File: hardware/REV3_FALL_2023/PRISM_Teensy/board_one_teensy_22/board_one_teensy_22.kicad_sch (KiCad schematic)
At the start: 19 parts, among them J1 EAST, J2 CORE_IO, J3 USB_micro, U1 Teensy4.1, U2 BNO055_Breakout, U3 3966

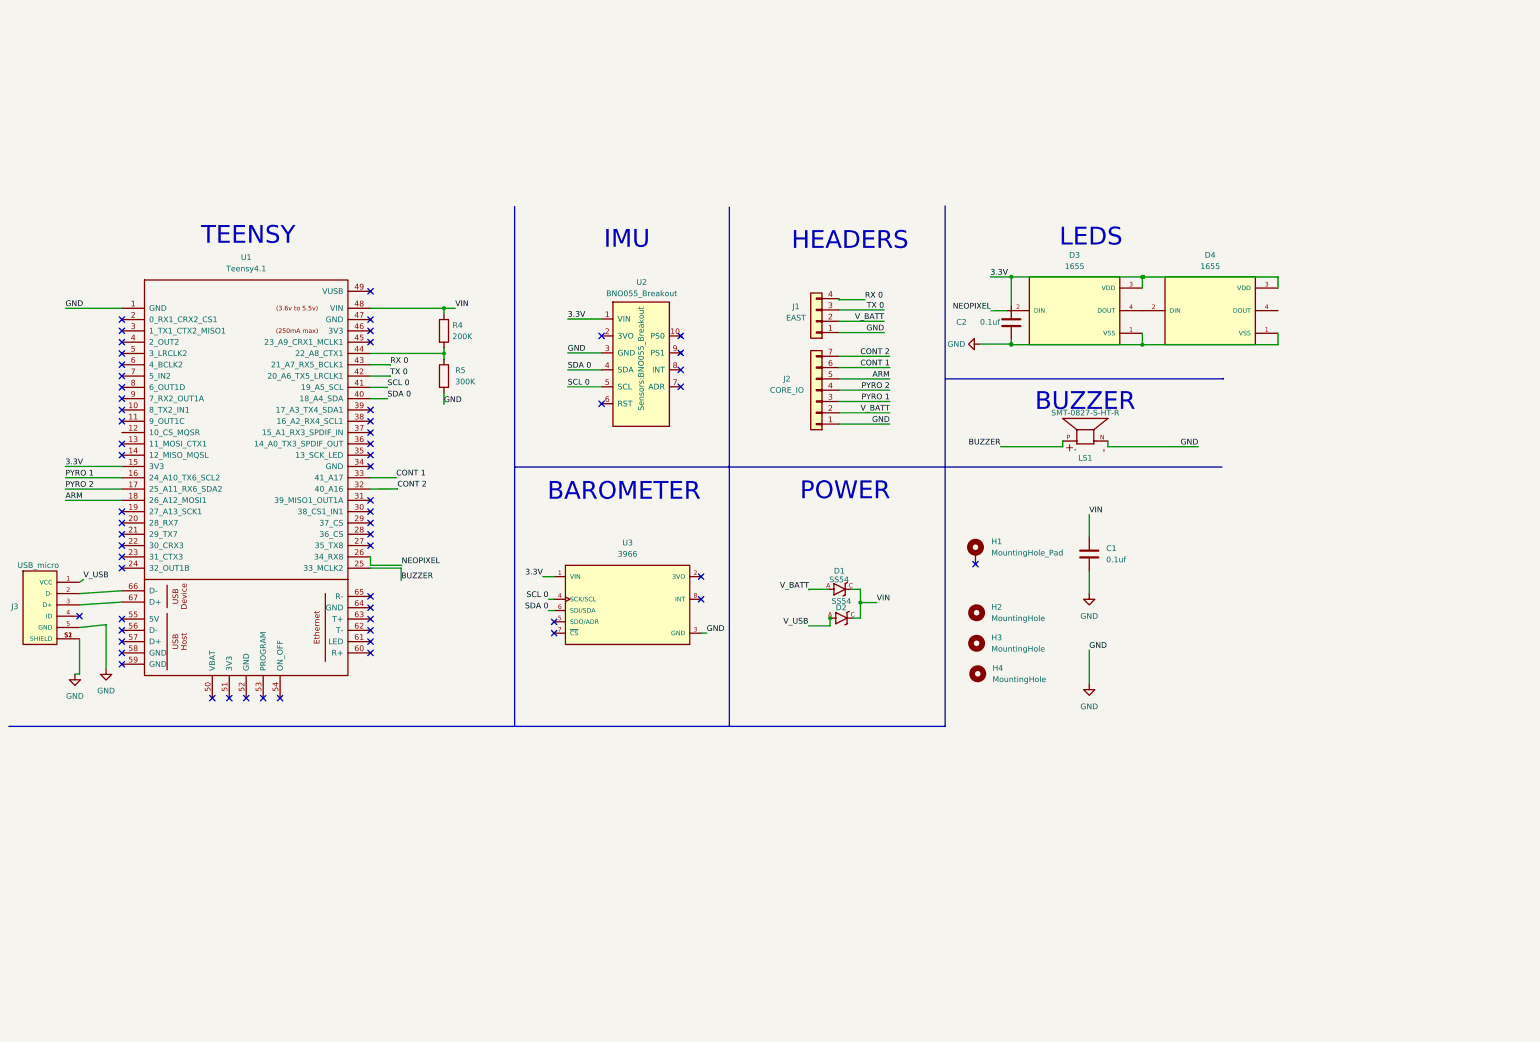
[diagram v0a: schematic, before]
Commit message: added teensy 4.0 and new connector spec
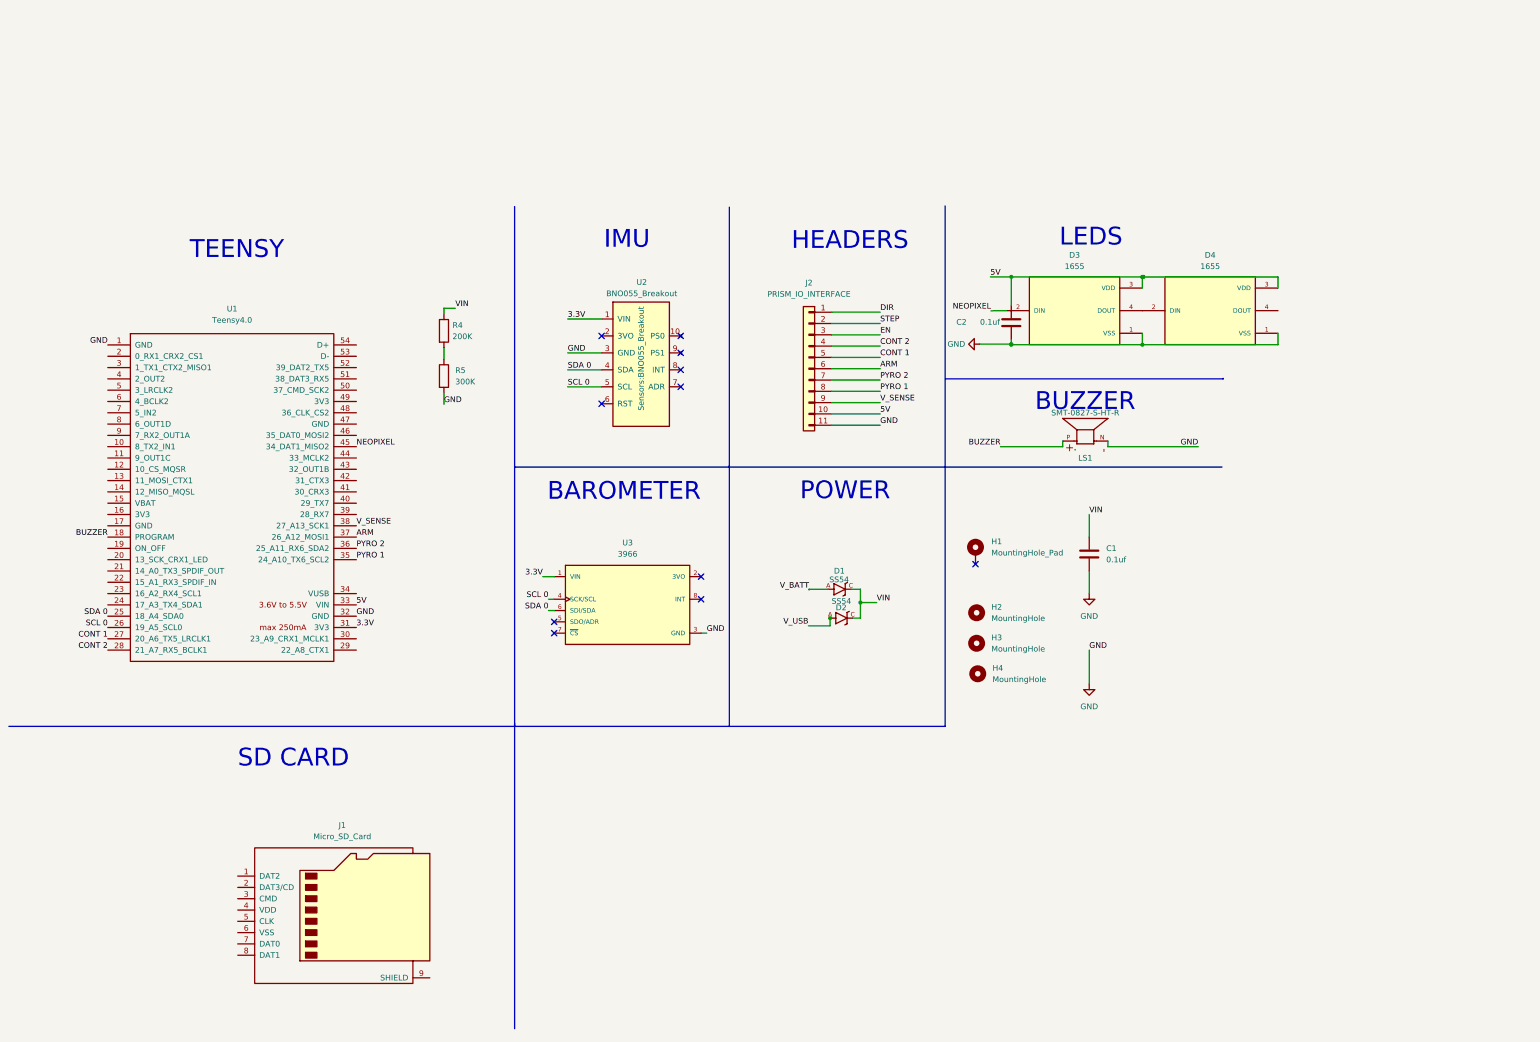
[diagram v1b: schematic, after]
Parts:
- removed J1: EAST, Connector_JST:JST_PH_S4B-PH-K_1x04_P2.00mm_Horizontal, symbol Connector_Generic:Conn_01x04
- removed J2: CORE_IO, Connector_JST:JST_PH_S7B-PH-K_1x07_P2.00mm_Horizontal, symbol Connector_Generic:Conn_01x07
- removed J3: USB_micro, USB:GCT_USB3131-30-0230-A_REVB, symbol USB:USB3131-30-0230-A_REVB
- removed U1: Teensy4.1, Teensy:Teensy41, symbol Teensy:Teensy4.1
- added J1: Micro_SD_Card, symbol Connector:Micro_SD_Card
- added J2: PRISM_IO_INTERFACE, symbol Connector_Generic:Conn_01x11
- added U1: Teensy4.0, Teensy_4.1:Teensy40, symbol Teensy_4.1:Teensy4.0
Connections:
- net 3.3V: now also U1.31 (3V3); no longer C2.2, D3.3 (VDD), D4.3 (VDD)
- net ARM: now also J2.6 (Pin_6), U1.37 (26_A12_MOSI1)
- net BUZZER: now also U1.18 (PROGRAM)
- net CONT 1: now also J2.5 (Pin_5), U1.27 (20_A6_TX5_LRCLK1)
- net CONT 2: now also J2.4 (Pin_4), U1.28 (21_A7_RX5_BCLK1)
- net GND: now also J2.11 (Pin_11), U1.1 (GND), U1.32 (GND)
- net NEOPIXEL: now also U1.45 (34_DAT1_MISO2)
- net PYRO 1: now also J2.8 (Pin_8), U1.35 (24_A10_TX6_SCL2)
- net PYRO 2: now also J2.7 (Pin_7), U1.36 (25_A11_RX6_SDA2)
- net SCL 0: now also U1.26 (19_A5_SCL0)
- net SDA 0: now also U1.25 (18_A4_SDA0)
- new net 5V: C2.2, D3.3 (VDD), D4.3 (VDD), J2.10 (Pin_10), U1.33 (VIN)
- new net DIR: J2.1 (Pin_1)
- new net EN: J2.3 (Pin_3)
- new net STEP: J2.2 (Pin_2)
- new net V_SENSE: J2.9 (Pin_9), U1.38 (27_A13_SCK1)
- no-connect marks 61 -> 11
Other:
- note added: "SD CARD"

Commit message: added footprint and symbol
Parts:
- removed J1: Micro_SD_Card, symbol Connector:Micro_SD_Card
- added J1: DM3CS-SF, DM3:HRS_DM3CS-SF, symbol DM3:DM3CS-SF
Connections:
- net 3.3V: now also J1.4 (VDD)
- net GND: now also J1.S1 (GND), J1.S2 (GND), J1.S3 (GND), J1.S5 (GND)
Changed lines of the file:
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@@
+    (effects (font (size 1.27 1.27)) (justify right bottom))
+  )
+  (label "3.3V" (at 67.31 149.86 180)
     (effects (font (size 1.27 1.27)) (justify right bottom))
   )
@@
   (label "SCL 0" (at 137.668 52.578 0)
     (effects (font (size 1.27 1.27)) (justify left bottom))
+  )
+  (label "GND" (at 67.31 180.34 180)
+    (effects (font (size 1.27 1.27)) (justify right bottom))
   )
   (symbol (lib_id "SS54:SS54") (at 198.7726 98.0826 0) (unit 1)
@@
     (pin "1")
   )
-  (symbol (lib_id "Connector:Micro_SD_Card") (at 86.36 170.18 0) (unit 1)
-    (in_bom yes) (on_board yes) (fields_autoplaced)
-    (property "Reference" "J1" (id 0) (at 86.995 151.13 0))
-    (property "Value" "Micro_SD_Card" (id 1) (at 86.995 153.67 0))
-    (property "Footprint" "" (id 2) (at 115.57 162.56 0)
-      (effects (font (size 1.27 1.27)) hide)
-    )
-    (property "Datasheet" "http://katalog.we-online.de/em/datasheet/693072010801.pdf" (id 3) (at 86.36 170.18 0)
-      (effects (font (size 1.27 1.27)) hide)
+  (symbol (lib_id "Device:SMT-0827-S-HT-R") (at 254 62.23 90) (unit 1)
+    (in_bom yes) (on_board yes)
+    (property "Reference" "LS1" (id 0) (at 254 68.58 90))
+    (property "Value" "SMT-0827-S-HT-R" (id 1) (at 254 58.42 90))
+    (property "Footprint" "buzzer:XDCR_SMT-0827-S-HT-R" (id 2) (at 242.57 62.23 0)
+      (effects (font (size 1.27 1.27)) (justify bottom) hide)
+    )
+    (property "Datasheet" "" (id 3) (at 254 62.23 0)
+      (effects (font (size 1.27 1.27)) hide)
+    )
+    (property "STANDARD" "Manufacturer Recommendations" (id 4) (at 243.84 62.23 0)
+      (effects (font (size 1.27 1.27)) (justify bottom) hide)
+    )
+    (property "MAXIMUM_PACKAGE_HEIGHT" "3.3mm" (id 5) (at 237.49 63.5 0)
+      (effects (font (size 1.27 1.27)) (justify bottom) hide)
+    )
+    (property "MANUFACTURER" "PUI Audio" (id 6) (at 238.76 63.5 0)
+      (effects (font (size 1.27 1.27)) (justify bottom) hide)
+    )
+    (property "PARTREV" "31/03/20" (id 7) (at 240.03 63.5 0)
+      (effects (font (size 1.27 1.27)) (justify bottom) hide)
+    )
+    (pin "N")
+    (pin "P")
+  )
+  (symbol (lib_id "Mechanical:MountingHole") (at 229.5755 103.3669 0) (unit 1)
+    (in_bom yes) (on_board yes) (fields_autoplaced)
+    (property "Reference" "H2" (id 0) (at 232.8775 102.0968 0)
+      (effects (font (size 1.27 1.27)) (justify left))
+    )
+    (property "Value" "MountingHole" (id 1) (at 232.8775 104.6368 0)
+      (effects (font (size 1.27 1.27)) (justify left))
+    )
+    (property "Footprint" "MountingHole:MountingHole_3.2mm_M3_DIN965_Pad_TopBottom" (id 2) (at 229.5755 103.3669 0)
+      (effects (font (size 1.27 1.27)) hide)
+    )
+    (property "Datasheet" "~" (id 3) (at 229.5755 103.3669 0))
+  )
+  (symbol (lib_id "Mechanical:MountingHole") (at 229.8295 117.0829 0) (unit 1)
+    (in_bom yes) (on_board yes) (fields_autoplaced)
+    (property "Reference" "H4" (id 0) (at 233.1315 115.8128 0)
+      (effects (font (size 1.27 1.27)) (justify left))
+    )
+    (property "Value" "MountingHole" (id 1) (at 233.1315 118.3528 0)
+      (effects (font (size 1.27 1.27)) (justify left))
+    )
+    (property "Footprint" "MountingHole:MountingHole_3.2mm_M3_DIN965_Pad_TopBottom" (id 2) (at 229.8295 117.0829 0)
+      (effects (font (size 1.27 1.27)) hide)
+    )
+    (property "Datasheet" "~" (id 3) (at 229.8295 117.0829 0))
+  )
+  (symbol (lib_id "DM3:DM3CS-SF") (at 80.01 165.1 0) (unit 1)
+    (in_bom yes) (on_board yes)
+    (property "Reference" "J1" (id 0) (at 88.9 163.8299 0)
+      (effects (font (size 1.27 1.27)) (justify left))
+    )
+    (property "Value" "DM3CS-SF" (id 1) (at 88.9 166.3699 0)
+      (effects (font (size 1.27 1.27)) (justify left))
+    )
+    (property "Footprint" "DM3:HRS_DM3CS-SF" (id 2) (at 99.06 160.02 0)
+      (effects (font (size 1.27 1.27)) (justify bottom))
+    )
+    (property "Datasheet" "" (id 3) (at 80.01 165.1 0)
+      (effects (font (size 1.27 1.27)) hide)
+    )
+    (property "MF" "Hirose" (id 4) (at 80.01 165.1 0)
+      (effects (font (size 1.27 1.27)) (justify bottom) hide)
+    )
+    (property "DESCRIPTION" "CONN MICRO SD CARD HINGED TYPE" (id 5) (at 80.01 165.1 0)
+      (effects (font (size 1.27 1.27)) (justify bottom) hide)
+    )
+    (property "PACKAGE" "None" (id 6) (at 80.01 165.1 0)
+      (effects (font (size 1.27 1.27)) (justify bottom) hide)
+    )
+    (property "PRICE" "1.14 USD" (id 7) (at 80.01 165.1 0)
+      (effects (font (size 1.27 1.27)) (justify bottom) hide)
+    )
+    (property "Package" "None" (id 8) (at 80.01 165.1 0)
+      (effects (font (size 1.27 1.27)) (justify bottom) hide)
+    )
+    (property "Check_prices" "https://www.snapeda.com/parts/DM3CS-SF/Hirose+Electric+Co+Ltd/view-part/?ref=eda" (id 9) (at 80.01 165.1 0)
+      (effects (font (size 1.27 1.27)) (justify bottom) hide)
+    )
+    (property "Availability" "In Stock" (id 10) (at 80.01 165.1 0)
+      (effects (font (size 1.27 1.27)) (justify bottom) hide)
+    )
+    (property "Price" "None" (id 11) (at 80.01 165.1 0)
+      (effects (font (size 1.27 1.27)) (justify bottom) hide)
+    )
+    (property "PARTREV" "n/a" (id 12) (at 80.01 165.1 0)
+      (effects (font (size 1.27 1.27)) (justify bottom) hide)
+    )
+    (property "SnapEDA_Link" "https://www.snapeda.com/parts/DM3CS-SF/Hirose+Electric+Co+Ltd/view-part/?ref=snap" (id 13) (at 80.01 165.1 0)
+      (effects (font (size 1.27 1.27)) (justify bottom) hide)
+    )
+    (property "MP" "DM3CS-SF" (id 14) (at 80.01 165.1 0)
+      (effects (font (size 1.27 1.27)) (justify bottom) hide)
+    )
+    (property "Purchase-URL" "https://www.snapeda.com/api/url_track_click_mouser/?unipart_id=189585&manufacturer=Hirose&part_name=DM3CS-SF&search_term=dm3cs-sf" (id 15) (at 80.01 165.1 0)
+      (effects (font (size 1.27 1.27)) (justify bottom) hide)
+    )
+    (property "Description" "\n10 (8 + 2) Position Card Connector Secure Digital - microSD™ Surface Mount, Right Angle Gold\n" (id 16) (at 80.01 165.1 0)
+      (effects (font (size 1.27 1.27)) (justify bottom) hide)
+    )
+    (property "STANDARED" "manufacturer recommendation" (id 17) (at 80.01 165.1 0)
+      (effects (font (size 1.27 1.27)) (justify bottom) hide)
+    )
+    (property "AVAILABILITY" "Good" (id 18) (at 80.01 165.1 0)
+      (effects (font (size 1.27 1.27)) (justify bottom) hide)
+    )
+    (property "MANUFACTURER" "Hirose" (id 19) (at 80.01 165.1 0)
+      (effects (font (size 1.27 1.27)) (justify bottom) hide)
     )
     (pin "1")
@@
     (pin "8")
     (pin "9")
-  )
-  (symbol (lib_id "Device:SMT-0827-S-HT-R") (at 254 62.23 90) (unit 1)
-    (in_bom yes) (on_board yes)
-    (property "Reference" "LS1" (id 0) (at 254 68.58 90))
-    (property "Value" "SMT-0827-S-HT-R" (id 1) (at 254 58.42 90))
-    (property "Footprint" "buzzer:XDCR_SMT-0827-S-HT-R" (id 2) (at 242.57 62.23 0)
-      (effects (font (size 1.27 1.27)) (justify bottom) hide)
-    )
-    (property "Datasheet" "" (id 3) (at 254 62.23 0)
-      (effects (font (size 1.27 1.27)) hide)
-    )
-    (property "STANDARD" "Manufacturer Recommendations" (id 4) (at 243.84 62.23 0)
-      (effects (font (size 1.27 1.27)) (justify bottom) hide)
-    )
-    (property "MAXIMUM_PACKAGE_HEIGHT" "3.3mm" (id 5) (at 237.49 63.5 0)
-      (effects (font (size 1.27 1.27)) (justify bottom) hide)
-    )
-    (property "MANUFACTURER" "PUI Audio" (id 6) (at 238.76 63.5 0)
-      (effects (font (size 1.27 1.27)) (justify bottom) hide)
-    )
-    (property "PARTREV" "31/03/20" (id 7) (at 240.03 63.5 0)
-      (effects (font (size 1.27 1.27)) (justify bottom) hide)
-    )
-    (pin "N")
-    (pin "P")
-  )
-  (symbol (lib_id "Mechanical:MountingHole") (at 229.5755 103.3669 0) (unit 1)
-    (in_bom yes) (on_board yes) (fields_autoplaced)
-    (property "Reference" "H2" (id 0) (at 232.8775 102.0968 0)
-      (effects (font (size 1.27 1.27)) (justify left))
-    )
-    (property "Value" "MountingHole" (id 1) (at 232.8775 104.6368 0)
-      (effects (font (size 1.27 1.27)) (justify left))
-    )
-    (property "Footprint" "MountingHole:MountingHole_3.2mm_M3_DIN965_Pad_TopBottom" (id 2) (at 229.5755 103.3669 0)
-      (effects (font (size 1.27 1.27)) hide)
-    )
-    (property "Datasheet" "~" (id 3) (at 229.5755 103.3669 0))
-  )
-  (symbol (lib_id "Mechanical:MountingHole") (at 229.8295 117.0829 0) (unit 1)
-    (in_bom yes) (on_board yes) (fields_autoplaced)
-    (property "Reference" "H4" (id 0) (at 233.1315 115.8128 0)
-      (effects (font (size 1.27 1.27)) (justify left))
-    )
-    (property "Value" "MountingHole" (id 1) (at 233.1315 118.3528 0)
-      (effects (font (size 1.27 1.27)) (justify left))
-    )
-    (property "Footprint" "MountingHole:MountingHole_3.2mm_M3_DIN965_Pad_TopBottom" (id 2) (at 229.8295 117.0829 0)
-      (effects (font (size 1.27 1.27)) hide)
-    )
-    (property "Datasheet" "~" (id 3) (at 229.8295 117.0829 0))
+    (pin "S1")
+    (pin "S2")
+    (pin "S3")
+    (pin "S5")
   )
   (symbol (lib_id "Device:C") (at 237.3686 38.165 180) (unit 1)
@@
       (reference "H4") (unit 1) (value "MountingHole") (footprint "MountingHole:MountingHole_3.2mm_M3_DIN965_Pad_TopBottom")
     )
-    (path "/6b183da5-8a39-4e17-8a9b-dcf7d6e2a229"
-      (reference "J1") (unit 1) (value "Micro_SD_Card") (footprint "")
+    (path "/852d1a41-0c32-42b5-87bd-1d71f536d8b5"
+      (reference "J1") (unit 1) (value "DM3CS-SF") (footprint "DM3:HRS_DM3CS-SF")
     )
     (path "/45cd3713-31a4-471f-8af8-e09906c7d903"

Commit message: add led
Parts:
- added D?: WS2812B, LED_SMD:LED_WS2812B_PLCC4_5.0x5.0mm_P3.2mm, symbol LED:WS2812B
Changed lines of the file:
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@@
+    (pin "4")
+  )
+  (symbol (lib_id "LED:WS2812B") (at 337.82 29.21 0) (unit 1)
+    (in_bom yes) (on_board yes) (fields_autoplaced)
+    (property "Reference" "D?" (id 0) (at 349.25 24.8793 0))
+    (property "Value" "WS2812B" (id 1) (at 349.25 27.4193 0))
+    (property "Footprint" "LED_SMD:LED_WS2812B_PLCC4_5.0x5.0mm_P3.2mm" (id 2) (at 339.09 36.83 0)
+      (effects (font (size 1.27 1.27)) (justify left top) hide)
+    )
+    (property "Datasheet" "https://cdn-shop.adafruit.com/datasheets/WS2812B.pdf" (id 3) (at 340.36 38.735 0)
+      (effects (font (size 1.27 1.27)) (justify left top) hide)
+    )
+    (pin "1")
+    (pin "2")
+    (pin "3")
     (pin "4")
   )
@@
       (reference "D4") (unit 1) (value "1655") (footprint "LED_1655")
     )
+    (path "/2bef43d4-e445-48f8-8183-402e18819c68"
+      (reference "D?") (unit 1) (value "WS2812B") (footprint "LED_SMD:LED_WS2812B_PLCC4_5.0x5.0mm_P3.2mm")
+    )
     (path "/635196a9-0bf5-4cbd-add4-521ce790d831"
